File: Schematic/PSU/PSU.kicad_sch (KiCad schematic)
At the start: 10 parts, among them J1 Conn_01x02, J3 Mains in, SW1 SW_SPDT

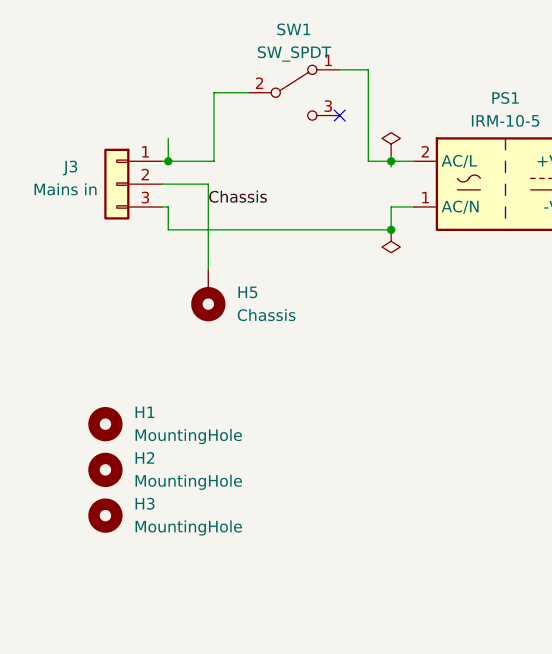
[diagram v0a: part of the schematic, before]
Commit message: Adjusted mounting hole position
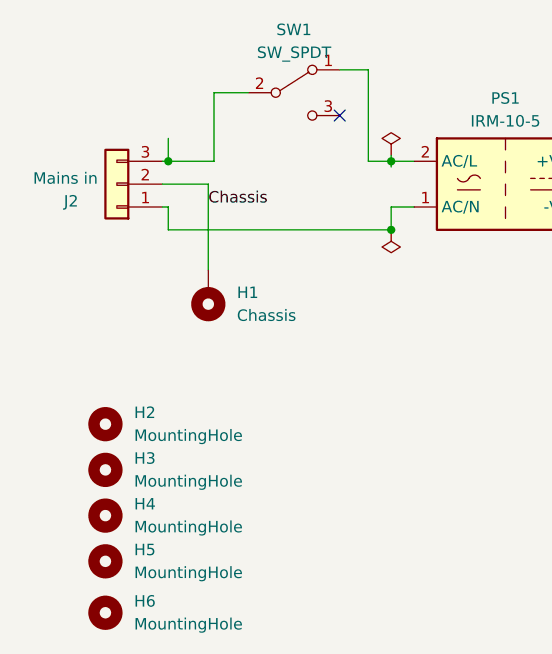
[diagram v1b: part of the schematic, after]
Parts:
- added H5, H6: MountingHole, MountingHole:MountingHole_3.2mm_M3, symbol Mechanical:MountingHole
- D1: footprint LED_THT:LED_D5.0mm -> myDevices:LED_Everlight_Side_1x2.1mm
- SW1: footprint myDevices:1101M1S3CQE2 -> myDevices:1101M2S3ABE2
- renumbered H5 to H1, H1 to H2, H2 to H3, H3 to H4, J3 to J2
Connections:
- net at J2.1 (Pin_1): now also PS1.1 (AC/N); no longer SW1.2 (B)
- net at J2.3 (Pin_3): now also SW1.2 (B); no longer PS1.1 (AC/N)
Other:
- moved on the sheet: J2
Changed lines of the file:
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@@
+    )
+  )
+  (netclass_flag "" (length 1) (shape round) (at 37.465 36.195 270) (fields_autoplaced)
+    (effects (font (size 1.27 1.27)) (justify right bottom))
+    (property "Netclass" "Mains" (at 38.465 35.4965 90)
+      (effects (font (size 1.27 1.27) italic) (justify left) hide)
     )
   )
@@
   (symbol (lib_id "Mechanical:MountingHole") (at 26.035 73.025 0) (unit 1)
     (in_bom yes) (on_board yes) (dnp no) (fields_autoplaced)
-    (property "Reference" "H3" (at 29.21 71.755 0)
+    (property "Reference" "H4" (at 29.21 71.755 0)
       (effects (font (size 1.27 1.27)) (justify left))
     )
@@
       (project "PSU"
         (path "/be906412-607c-4356-b276-4619dcf8dbfd"
-          (reference "H3") (unit 1)
+          (reference "H4") (unit 1)
         )
       )
@@
       (effects (font (size 1.27 1.27)) hide)
     )
-    (property "Footprint" "LED_THT:LED_D5.0mm" (at 91.44 33.655 0)
+    (property "Footprint" "myDevices:LED_Everlight_Side_1x2.1mm" (at 91.44 33.655 0)
       (effects (font (size 1.27 1.27)) hide)
     )
@@
     )
   )
-  (symbol (lib_id "Connector_Generic:Conn_01x03") (at 27.305 36.195 0) (mirror y) (unit 1)
-    (in_bom yes) (on_board yes) (dnp no)
-    (property "Reference" "J3" (at 22.225 34.29 0)
-      (effects (font (size 1.27 1.27)))
-    )
-    (property "Value" "Mains in" (at 21.59 36.83 0)
+  (symbol (lib_id "Connector_Generic:Conn_01x03") (at 27.305 36.195 180) (unit 1)
+    (in_bom yes) (on_board yes) (dnp no)
+    (property "Reference" "J2" (at 22.225 38.1 0)
+      (effects (font (size 1.27 1.27)))
+    )
+    (property "Value" "Mains in" (at 21.59 35.56 0)
       (effects (font (size 1.27 1.27)))
     )
@@
       (project "PSU"
         (path "/be906412-607c-4356-b276-4619dcf8dbfd"
-          (reference "J3") (unit 1)
+          (reference "J2") (unit 1)
         )
       )
@@
   (symbol (lib_id "Mechanical:MountingHole_Pad") (at 37.465 48.26 180) (unit 1)
     (in_bom yes) (on_board yes) (dnp no) (fields_autoplaced)
-    (property "Reference" "H5" (at 40.64 48.26 0)
+    (property "Reference" "H1" (at 40.64 48.26 0)
       (effects (font (size 1.27 1.27)) (justify right))
     )
@@
       (project "PSU"
         (path "/be906412-607c-4356-b276-4619dcf8dbfd"
-          (reference "H5") (unit 1)
+          (reference "H1") (unit 1)
         )
       )
@@
   (symbol (lib_id "power:GND") (at 83.82 46.99 0) (unit 1)
     (in_bom yes) (on_board yes) (dnp no)
-    (property "Reference" "#PWR03" (at 83.82 53.34 0)
+    (property "Reference" "#PWR02" (at 83.82 53.34 0)
       (effects (font (size 1.27 1.27)) hide)
     )
@@
       (project "PSU"
         (path "/be906412-607c-4356-b276-4619dcf8dbfd"
-          (reference "#PWR03") (unit 1)
+          (reference "#PWR02") (unit 1)
         )
       )
@@
   (symbol (lib_id "Mechanical:MountingHole") (at 26.035 62.865 0) (unit 1)
     (in_bom yes) (on_board yes) (dnp no) (fields_autoplaced)
-    (property "Reference" "H1" (at 29.21 61.595 0)
+    (property "Reference" "H2" (at 29.21 61.595 0)
       (effects (font (size 1.27 1.27)) (justify left))
     )
@@
       (project "PSU"
         (path "/be906412-607c-4356-b276-4619dcf8dbfd"
-          (reference "H1") (unit 1)
+          (reference "H2") (unit 1)
+        )
+      )
+    )
+  )
+  (symbol (lib_id "Mechanical:MountingHole") (at 26.035 83.82 0) (unit 1)
+    (in_bom yes) (on_board yes) (dnp no) (fields_autoplaced)
+    (property "Reference" "H6" (at 29.21 82.55 0)
+      (effects (font (size 1.27 1.27)) (justify left))
+    )
+    (property "Value" "MountingHole" (at 29.21 85.09 0)
+      (effects (font (size 1.27 1.27)) (justify left))
+    )
+    (property "Footprint" "MountingHole:MountingHole_3.2mm_M3" (at 26.035 83.82 0)
+      (effects (font (size 1.27 1.27)) hide)
+    )
+    (property "Datasheet" "~" (at 26.035 83.82 0)
+      (effects (font (size 1.27 1.27)) hide)
+    )
+    (property "Comments" "" (at 26.035 83.82 0)
+      (effects (font (size 1.27 1.27)))
+    )
+    (instances
+      (project "PSU"
+        (path "/be906412-607c-4356-b276-4619dcf8dbfd"
+          (reference "H6") (unit 1)
         )
       )
@@
       (effects (font (size 1.27 1.27)))
     )
-    (property "Footprint" "myDevices:1101M1S3CQE2" (at 46.99 26.035 0)
+    (property "Footprint" "myDevices:1101M2S3ABE2" (at 46.99 26.035 0)
       (effects (font (size 1.27 1.27)) hide)
     )
@@
   (symbol (lib_id "Mechanical:MountingHole") (at 26.035 67.945 0) (unit 1)
     (in_bom yes) (on_board yes) (dnp no) (fields_autoplaced)
-    (property "Reference" "H2" (at 29.21 66.675 0)
+    (property "Reference" "H3" (at 29.21 66.675 0)
       (effects (font (size 1.27 1.27)) (justify left))
     )
@@
       (project "PSU"
         (path "/be906412-607c-4356-b276-4619dcf8dbfd"
-          (reference "H2") (unit 1)
+          (reference "H3") (unit 1)
         )
       )
@@
         )
       )
+    )
+  )
+  (symbol (lib_id "Mechanical:MountingHole") (at 26.035 78.105 0) (unit 1)
+    (in_bom yes) (on_board yes) (dnp no) (fields_autoplaced)
+    (property "Reference" "H5" (at 29.21 76.835 0)
+      (effects (font (size 1.27 1.27)) (justify left))
+    )
+    (property "Value" "MountingHole" (at 29.21 79.375 0)
+      (effects (font (size 1.27 1.27)) (justify left))
+    )
+    (property "Footprint" "MountingHole:MountingHole_3.2mm_M3" (at 26.035 78.105 0)
+      (effects (font (size 1.27 1.27)) hide)
+    )
+    (property "Datasheet" "~" (at 26.035 78.105 0)
+      (effects (font (size 1.27 1.27)) hide)
+    )
+    (property "Comments" "" (at 26.035 78.105 0)
+      (effects (font (size 1.27 1.27)))
+    )
+    (instances
+      (project "PSU"
+        (path "/be906412-607c-4356-b276-4619dcf8dbfd"
+          (reference "H5") (unit 1)
+        )
+      )

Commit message: Updated production files
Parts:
- D1: value LED -> Everlight 27-21/R6C-AM2N2LY/3C
- J1: value Conn_01x02 -> 5V output; footprint myDevices:KF2510-2P -> Connector_Molex:Molex_KK-254_AE-6410-02A_1x02_P2.54mm_Vertical
- J2: footprint myDevices:TerminalBlock_LCSC_P5.08mm_3 -> Retronics_Connectors:ScrewTerminal_DB128L-5.08-3P-BK-S
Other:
- moved on the sheet: H2, H3, H4, H5, H6
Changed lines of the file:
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@@
     )
   )
-  (symbol (lib_id "Mechanical:MountingHole") (at 26.035 73.025 0) (unit 1)
-    (in_bom yes) (on_board yes) (dnp no) (fields_autoplaced)
-    (property "Reference" "H4" (at 29.21 71.755 0)
-      (effects (font (size 1.27 1.27)) (justify left))
-    )
-    (property "Value" "MountingHole" (at 29.21 74.295 0)
-      (effects (font (size 1.27 1.27)) (justify left))
-    )
-    (property "Footprint" "MountingHole:MountingHole_3.2mm_M3" (at 26.035 73.025 0)
-      (effects (font (size 1.27 1.27)) hide)
-    )
-    (property "Datasheet" "~" (at 26.035 73.025 0)
-      (effects (font (size 1.27 1.27)) hide)
-    )
-    (property "Comments" "" (at 26.035 73.025 0)
+  (symbol (lib_id "Mechanical:MountingHole") (at 153.67 178.435 0) (unit 1)
+    (in_bom yes) (on_board yes) (dnp no) (fields_autoplaced)
+    (property "Reference" "H4" (at 156.845 177.165 0)
+      (effects (font (size 1.27 1.27)) (justify left))
+    )
+    (property "Value" "MountingHole" (at 156.845 179.705 0)
+      (effects (font (size 1.27 1.27)) (justify left))
+    )
+    (property "Footprint" "MountingHole:MountingHole_3.2mm_M3" (at 153.67 178.435 0)
+      (effects (font (size 1.27 1.27)) hide)
+    )
+    (property "Datasheet" "~" (at 153.67 178.435 0)
+      (effects (font (size 1.27 1.27)) hide)
+    )
+    (property "Comments" "" (at 153.67 178.435 0)
       (effects (font (size 1.27 1.27)))
     )
@@
       (effects (font (size 1.27 1.27)))
     )
-    (property "Value" "LED" (at 93.0275 28.575 0)
+    (property "Value" "Everlight 27-21/R6C-AM2N2LY/3C" (at 93.0275 28.575 0)
       (effects (font (size 1.27 1.27)) hide)
     )
@@
       (effects (font (size 1.27 1.27)))
     )
-    (property "Footprint" "myDevices:TerminalBlock_LCSC_P5.08mm_3" (at 27.305 36.195 0)
+    (property "Footprint" "Retronics_Connectors:ScrewTerminal_DB128L-5.08-3P-BK-S" (at 27.305 36.195 0)
       (effects (font (size 1.27 1.27)) hide)
     )
@@
     )
   )
-  (symbol (lib_id "Mechanical:MountingHole") (at 26.035 62.865 0) (unit 1)
-    (in_bom yes) (on_board yes) (dnp no) (fields_autoplaced)
-    (property "Reference" "H2" (at 29.21 61.595 0)
-      (effects (font (size 1.27 1.27)) (justify left))
-    )
-    (property "Value" "MountingHole" (at 29.21 64.135 0)
-      (effects (font (size 1.27 1.27)) (justify left))
-    )
-    (property "Footprint" "MountingHole:MountingHole_3.2mm_M3" (at 26.035 62.865 0)
-      (effects (font (size 1.27 1.27)) hide)
-    )
-    (property "Datasheet" "~" (at 26.035 62.865 0)
-      (effects (font (size 1.27 1.27)) hide)
-    )
-    (property "Comments" "" (at 26.035 62.865 0)
+  (symbol (lib_id "Mechanical:MountingHole") (at 153.67 168.275 0) (unit 1)
+    (in_bom yes) (on_board yes) (dnp no) (fields_autoplaced)
+    (property "Reference" "H2" (at 156.845 167.005 0)
+      (effects (font (size 1.27 1.27)) (justify left))
+    )
+    (property "Value" "MountingHole" (at 156.845 169.545 0)
+      (effects (font (size 1.27 1.27)) (justify left))
+    )
+    (property "Footprint" "MountingHole:MountingHole_3.2mm_M3" (at 153.67 168.275 0)
+      (effects (font (size 1.27 1.27)) hide)
+    )
+    (property "Datasheet" "~" (at 153.67 168.275 0)
+      (effects (font (size 1.27 1.27)) hide)
+    )
+    (property "Comments" "" (at 153.67 168.275 0)
       (effects (font (size 1.27 1.27)))
     )
@@
     )
   )
-  (symbol (lib_id "Mechanical:MountingHole") (at 26.035 83.82 0) (unit 1)
-    (in_bom yes) (on_board yes) (dnp no) (fields_autoplaced)
-    (property "Reference" "H6" (at 29.21 82.55 0)
-      (effects (font (size 1.27 1.27)) (justify left))
-    )
-    (property "Value" "MountingHole" (at 29.21 85.09 0)
-      (effects (font (size 1.27 1.27)) (justify left))
-    )
-    (property "Footprint" "MountingHole:MountingHole_3.2mm_M3" (at 26.035 83.82 0)
-      (effects (font (size 1.27 1.27)) hide)
-    )
-    (property "Datasheet" "~" (at 26.035 83.82 0)
-      (effects (font (size 1.27 1.27)) hide)
-    )
-    (property "Comments" "" (at 26.035 83.82 0)
+  (symbol (lib_id "Mechanical:MountingHole") (at 153.67 189.23 0) (unit 1)
+    (in_bom yes) (on_board yes) (dnp no) (fields_autoplaced)
+    (property "Reference" "H6" (at 156.845 187.96 0)
+      (effects (font (size 1.27 1.27)) (justify left))
+    )
+    (property "Value" "MountingHole" (at 156.845 190.5 0)
+      (effects (font (size 1.27 1.27)) (justify left))
+    )
+    (property "Footprint" "MountingHole:MountingHole_3.2mm_M3" (at 153.67 189.23 0)
+      (effects (font (size 1.27 1.27)) hide)
+    )
+    (property "Datasheet" "~" (at 153.67 189.23 0)
+      (effects (font (size 1.27 1.27)) hide)
+    )
+    (property "Comments" "" (at 153.67 189.23 0)
       (effects (font (size 1.27 1.27)))
     )
@@
       (effects (font (size 1.27 1.27)) (justify left))
     )
-    (property "Value" "Conn_01x02" (at 109.22 37.465 0)
-      (effects (font (size 1.27 1.27)) (justify left))
-    )
-    (property "Footprint" "myDevices:KF2510-2P" (at 106.68 34.925 0)
+    (property "Value" "5V output" (at 109.22 37.465 0)
+      (effects (font (size 1.27 1.27)) (justify left))
+    )
+    (property "Footprint" "Connector_Molex:Molex_KK-254_AE-6410-02A_1x02_P2.54mm_Vertical" (at 106.68 34.925 0)
       (effects (font (size 1.27 1.27)) hide)
     )
@@
     )
   )
-  (symbol (lib_id "Mechanical:MountingHole") (at 26.035 67.945 0) (unit 1)
-    (in_bom yes) (on_board yes) (dnp no) (fields_autoplaced)
-    (property "Reference" "H3" (at 29.21 66.675 0)
-      (effects (font (size 1.27 1.27)) (justify left))
-    )
-    (property "Value" "MountingHole" (at 29.21 69.215 0)
-      (effects (font (size 1.27 1.27)) (justify left))
-    )
-    (property "Footprint" "MountingHole:MountingHole_3.2mm_M3" (at 26.035 67.945 0)
-      (effects (font (size 1.27 1.27)) hide)
-    )
-    (property "Datasheet" "~" (at 26.035 67.945 0)
-      (effects (font (size 1.27 1.27)) hide)
-    )
-    (property "Comments" "" (at 26.035 67.945 0)
+  (symbol (lib_id "Mechanical:MountingHole") (at 153.67 173.355 0) (unit 1)
+    (in_bom yes) (on_board yes) (dnp no) (fields_autoplaced)
+    (property "Reference" "H3" (at 156.845 172.085 0)
+      (effects (font (size 1.27 1.27)) (justify left))
+    )
+    (property "Value" "MountingHole" (at 156.845 174.625 0)
+      (effects (font (size 1.27 1.27)) (justify left))
+    )
+    (property "Footprint" "MountingHole:MountingHole_3.2mm_M3" (at 153.67 173.355 0)
+      (effects (font (size 1.27 1.27)) hide)
+    )
+    (property "Datasheet" "~" (at 153.67 173.355 0)
+      (effects (font (size 1.27 1.27)) hide)
+    )
+    (property "Comments" "" (at 153.67 173.355 0)
       (effects (font (size 1.27 1.27)))
     )
@@
     )
   )
-  (symbol (lib_id "Mechanical:MountingHole") (at 26.035 78.105 0) (unit 1)
-    (in_bom yes) (on_board yes) (dnp no) (fields_autoplaced)
-    (property "Reference" "H5" (at 29.21 76.835 0)
-      (effects (font (size 1.27 1.27)) (justify left))
-    )
-    (property "Value" "MountingHole" (at 29.21 79.375 0)
-      (effects (font (size 1.27 1.27)) (justify left))
-    )
-    (property "Footprint" "MountingHole:MountingHole_3.2mm_M3" (at 26.035 78.105 0)
-      (effects (font (size 1.27 1.27)) hide)
-    )
-    (property "Datasheet" "~" (at 26.035 78.105 0)
-      (effects (font (size 1.27 1.27)) hide)
-    )
-    (property "Comments" "" (at 26.035 78.105 0)
-      (effects (font (size 1.27 1.27)))
-    )
+  (symbol (lib_id "Mechanical:MountingHole") (at 153.67 183.515 0) (unit 1)
+    (in_bom yes) (on_board yes) (dnp no) (fields_autoplaced)
+    (property "Reference" "H5" (at 156.845 182.245 0)
+      (effects (font (size 1.27 1.27)) (justify left))
+    )
+    (property "Value" "MountingHole" (at 156.845 184.785 0)
+      (effects (font (size 1.27 1.27)) (justify left))
+    )
+    (property "Footprint" "MountingHole:MountingHole_3.2mm_M3" (at 153.67 183.515 0)
+      (effects (font (size 1.27 1.27)) hide)
+    )
+    (property "Datasheet" "~" (at 153.67 183.515 0)
+      (effects (font (size 1.27 1.27)) hide)
+    )
+    (property "Comments" "" (at 153.67 183.515 0)
+      (effects (font (size 1.27 1.27)))
+    )
